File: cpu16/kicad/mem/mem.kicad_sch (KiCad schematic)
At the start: 16 parts, among them J2 BACKPLANE_2x32, U116 74HC688, U117 74HC688, U118 62256, U119 62256, U120 74HC574, U142 74HC32, U161 74HC04

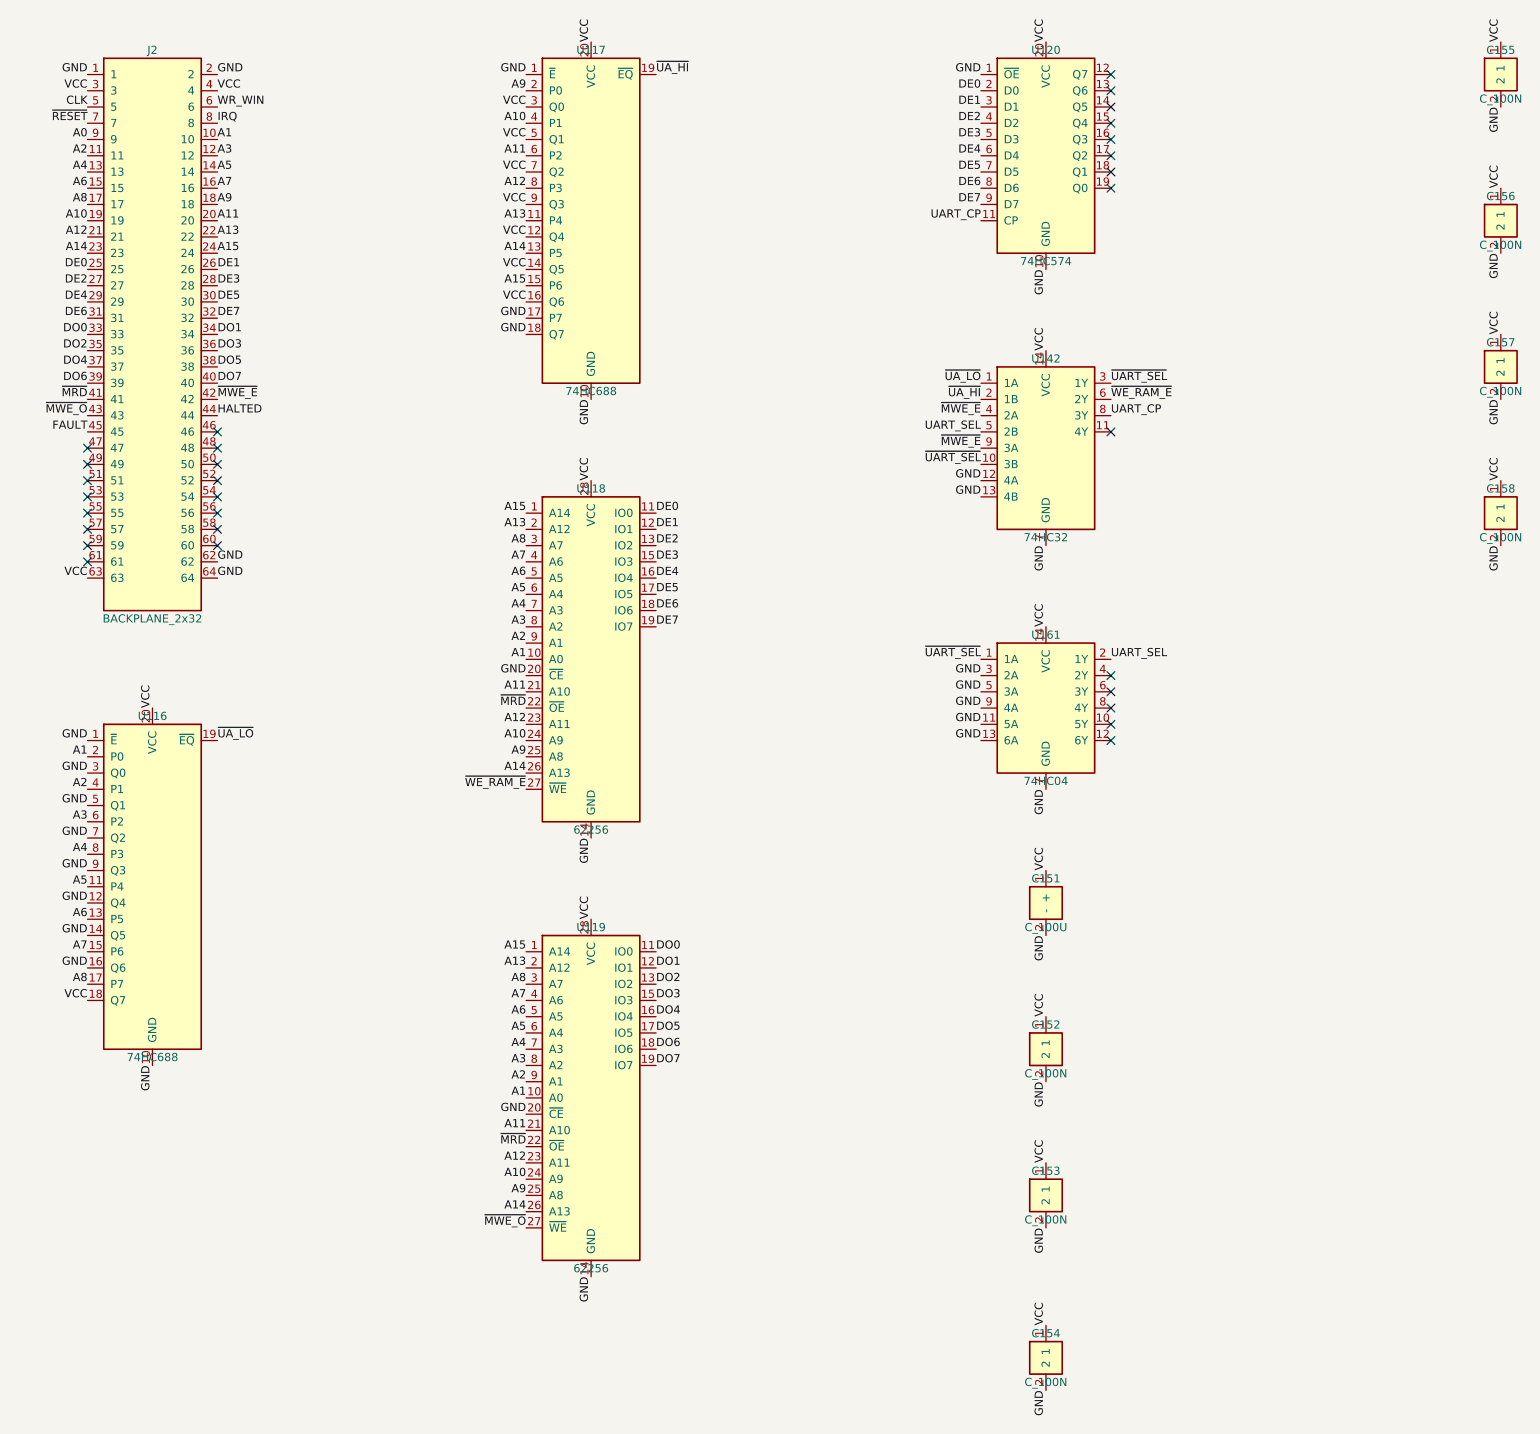
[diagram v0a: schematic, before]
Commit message: Kart başına kararlı referans numaraları; yapıştırıcı kapı ve pasiflerde blok bilgisi
Her kart kendi KiCad projesi olduğu için numaralar kart içinde verilir (cpu U1.., clk U201..,
mem U301..). Deney rehberi bir bloğun hangi kapı birimlerini kullandığını bilsin diye yapıştırıcı
lojik çiplerine birim → blok eşlemesi eklendi.

Co-Authored-By: Claude Opus 5.5 (1M context) <noreply@anthropic.com>
Claude-Session: https://claude.ai/code/session_018J8WVuECVRbQJyCbmF6Nsi
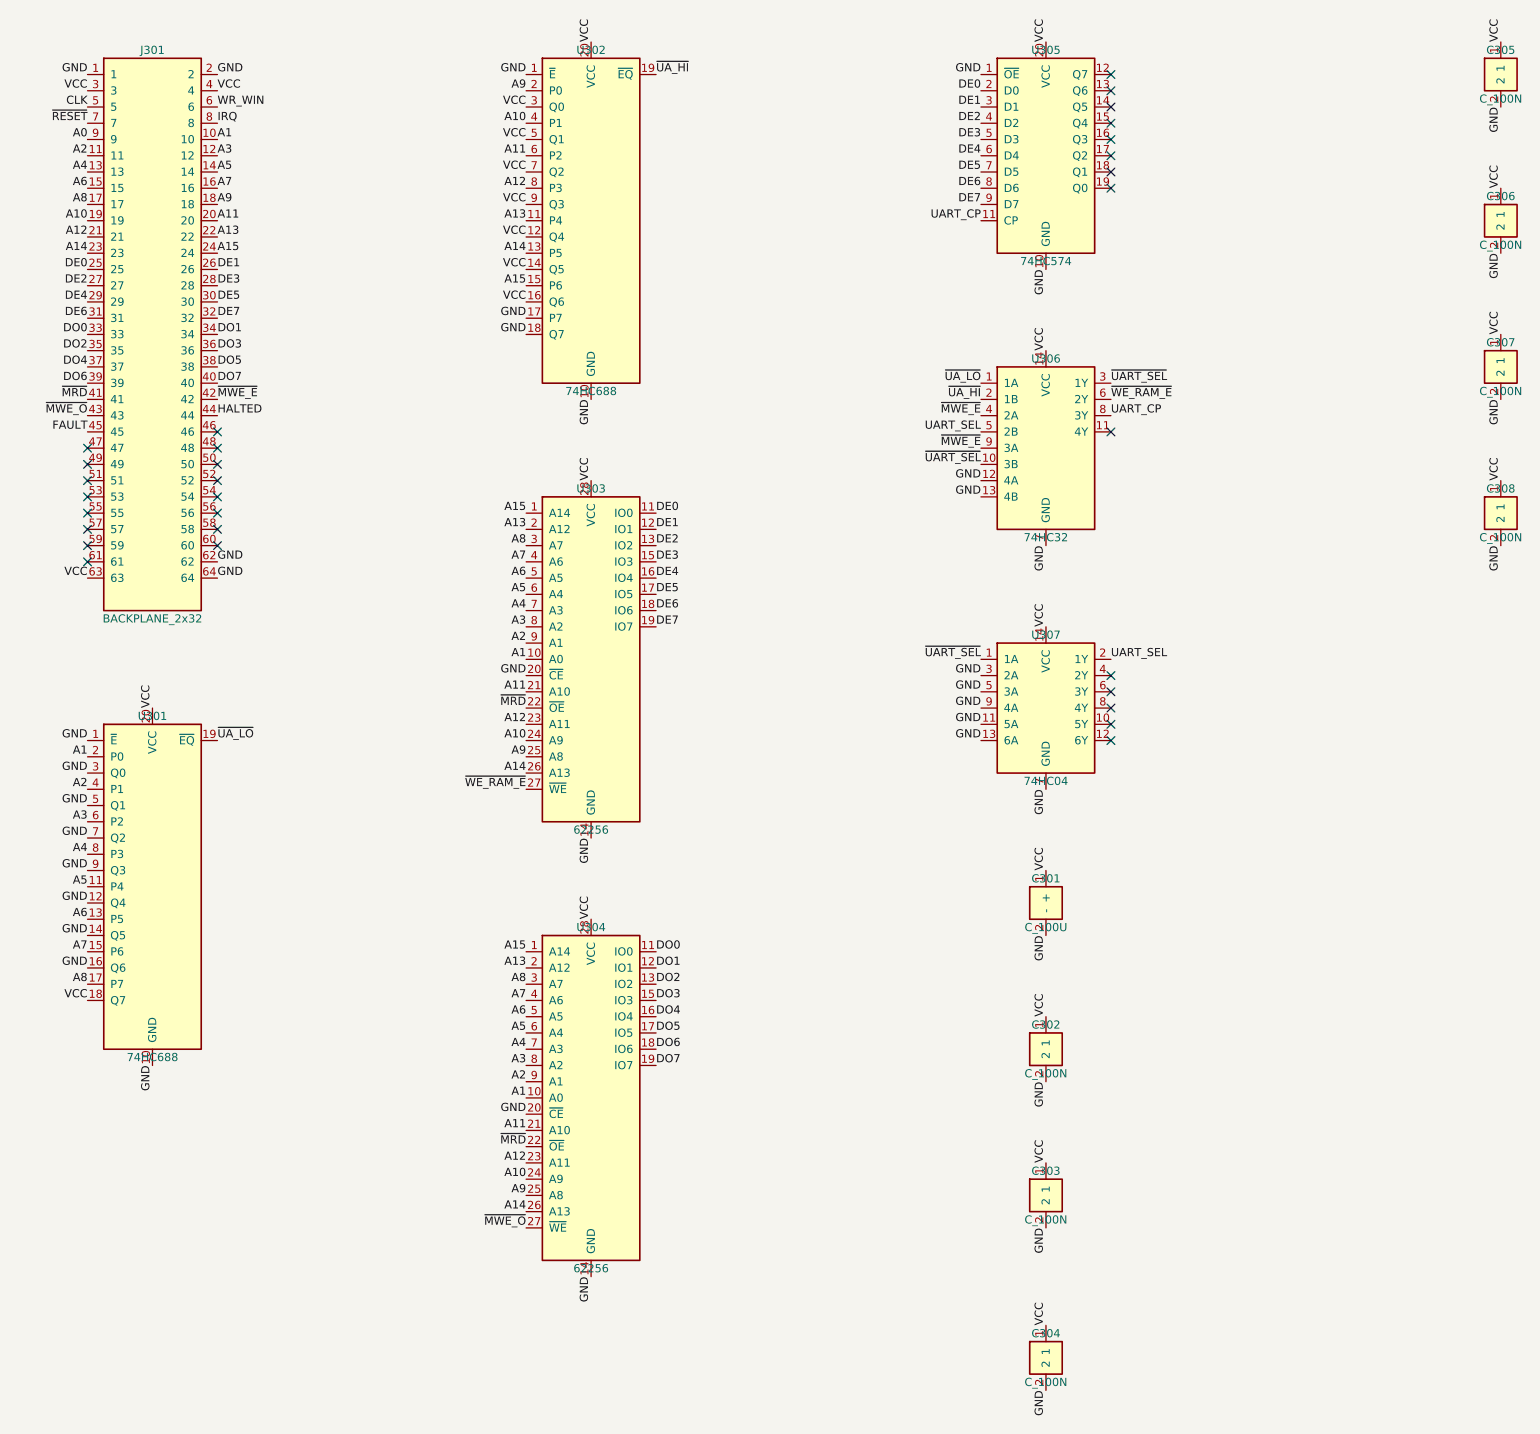
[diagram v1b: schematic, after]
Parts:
- C302: renamed from C152; Gorev U116 dekuplaj -> U301 dekuplaj
- C303: renamed from C153; Gorev U117 dekuplaj -> U302 dekuplaj
- C304: renamed from C154; Gorev U118 dekuplaj -> U303 dekuplaj
- C305: renamed from C155; Gorev U119 dekuplaj -> U304 dekuplaj
- C306: renamed from C156; Gorev U120 dekuplaj -> U305 dekuplaj
- C307: renamed from C157; Gorev U142 dekuplaj -> U306 dekuplaj
- C308: renamed from C158; Gorev U161 dekuplaj -> U307 dekuplaj
- renumbered C151 to C301, J2 to J301, U116 to U301, U117 to U302, U118 to U303, U119 to U304, U120 to U305, U142 to U306, U161 to U307
